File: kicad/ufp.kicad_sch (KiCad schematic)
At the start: 6 parts, among them J2 SS-52400-003

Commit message: Some random tildas added by default for some reason
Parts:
- C1: value (none) -> ~
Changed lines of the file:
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@@
       (effects (font (size 1.27 1.27)) (justify right))
     )
-    (property "Value" "" (id 1) (at 97.79 93.9862 0)
+    (property "Value" "~" (id 1) (at 97.79 93.9862 0)
       (effects (font (size 1.27 1.27)) (justify right))
     )

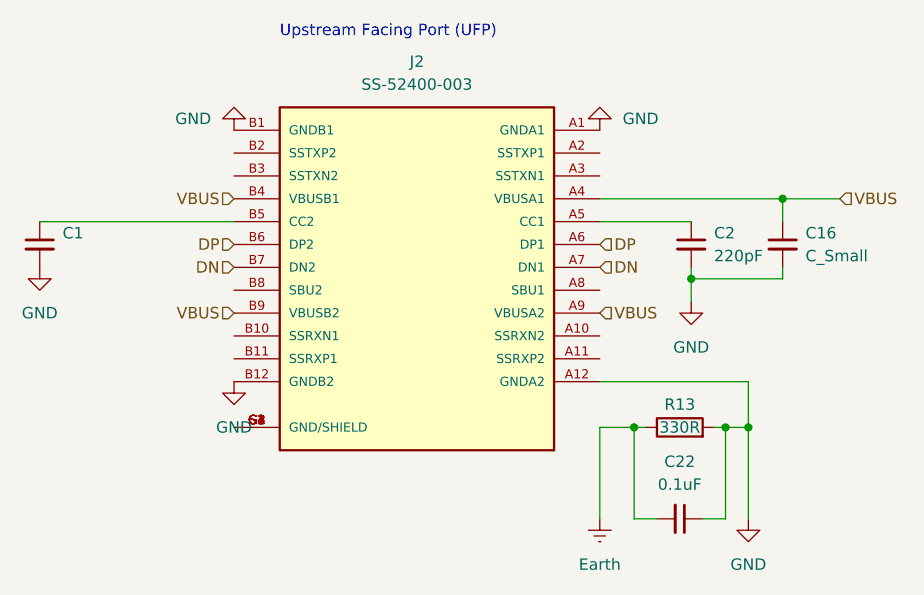
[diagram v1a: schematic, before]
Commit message: Some overwritten changes by swapping back to robot project
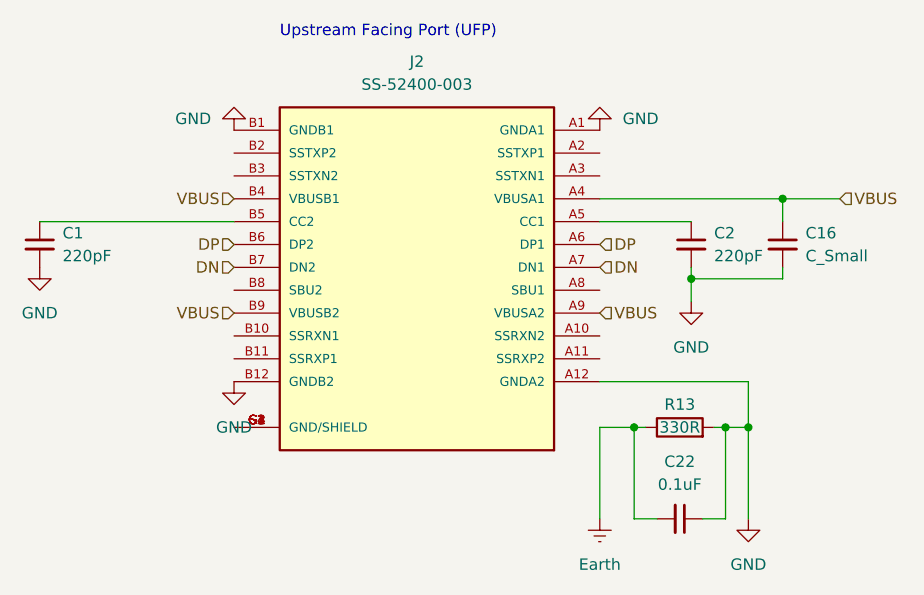
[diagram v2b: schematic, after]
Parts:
- C1: value ~ -> 220pF; footprint (none) -> Capacitor_SMD:C_0402_1005Metric
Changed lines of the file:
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@@
       (effects (font (size 1.27 1.27)) (justify right))
     )
-    (property "Value" "~" (id 1) (at 97.79 93.9862 0)
+    (property "Value" "220pF" (id 1) (at 97.79 93.9862 0)
       (effects (font (size 1.27 1.27)) (justify right))
     )
-    (property "Footprint" "" (id 2) (at 95.25 92.71 0)
+    (property "Footprint" "Capacitor_SMD:C_0402_1005Metric" (id 2) (at 95.25 92.71 0)
       (effects (font (size 1.27 1.27)) hide)
     )
